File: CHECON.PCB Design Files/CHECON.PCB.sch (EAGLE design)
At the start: 24 parts, among them U2 MAX232SOIC16, U3 RS485SOIC

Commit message: CHECON.PCB.v1.0 pre-release
Pending checklist processing.
Added all part and manufacturer numbers, fiducials, silkscreen
labelling, BOM, ECO, FAB notes, Gerber files (+ drill and centroid)
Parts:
- added IC1: (no value), KW2:NCP1117ST33T3G_1
- added U$17, U$34: 1uF, GW-devices:RF-C0805
- added U$24, U$31, U$32, U$35: 10uF, GW-devices:RF-C0805
- added U$25, U$26, U$27, U$28, U$29, U$6: 10k, GW-devices:RF-R0805
- added U$30: RA_BUTTON, KW2:RA_BUTTON
- added U$33, U$7: 0.1uF, GW-devices:RF-C0805
- added U$36: 0, GW-devices:RF-R0805
- added U$37: DIODE-ZENER-BZT52, SparkFun:DIODE-ZENER-BZT52
- added U$38, U$39, U$40, U$41, U$42, U$43: FIDUCIAL, adafruit:FIDUCIAL
- POSCON: MFGN (none) -> Molex; MFGP (none) -> 0955016889
- SCANNER: MFGP (none) -> 0955016889
- U$1: MFGP (none) -> CLV1A-FKB-CK1N1G1BB7R4S3
- U$10: MFGP (none) -> DF12(3.0)-40DP-0.5V(86)
- U$11, U$12, U$21, U$22, U$23: value (none) -> 1uF; MFGN (none) -> TDK; MFGP (none) -> C2012X5R1E105K125AA
- U$13, U$14, U$15, U$16: MFGN (none) -> E-Switch; MFGP (none) -> TL3301DF160QG
- U$18, U$19, U$20: value (none) -> 24; MFGN (none) -> Vishay Dale; MFGP (none) -> CRCW080524R0FKEA
- U$2: value 52745-1097 -> (none); MFGP (none) -> 52745-1097
- U$3: MFGP (none) -> 3220-20-0100-00
- U$8: MFGP (none) -> WS2801
- U$9: MFGP (none) -> PJ-002A
- U2, U3: MFGN TI -> (none)
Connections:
- new net N$32: U$2.EXTMODE, U$6.1
- new net N$33: U$2.EXCOMIN, U$25.1
- new net N$34: U$10.PTE2/LLWU_P1/MADC0_DP1/SPI1_SCK/!UART1_CTS!/MTRACE_D2, U$16.4, U$26.1
- new net N$35: U$10.PTE17/ADC0_SE5A/SPI0_SCK/UART2_RX/FTM_CLKIN1/LPTMR0_ALT3, U$15.4, U$27.1
- new net N$36: U$10.PTE4/LLWU_P2/SPI1_PCS0/MTRACE_D0, U$14.4, U$28.1
- new net N$37: U$10.PTE16/ADC0_SE4A/SPI0_PCS0/UART2_TX/FTM_CLKIN0/FTM0_FLT3, U$13.4, U$29.1
- new net N$39: U$10.PTD4/LLWU_P14/MADC0_SE21/SPI0_PCS1/!UART0_RTS!/FTM0_CH4/EWM_IN/GPIO_BSM_FRAME, U$5.EN
- new net N$40: U$10.PTD3/SPI0_SIN/UART2_TX/I2C0_SCL/GPIO5_BSM_CLK, U$4.EN
- new net N$41: U$10.PTE3/MADC0_DM1/SPI1_SIN/!UART1_RTS!/MTRACE_D1/SPI1_SOUT, U2.T2IN
- new net OUT1: IC1.OUT, IC1.OUT1, U$32.2, U$36.1
- net +3V3: now also U$21.1, U$26.2, U$27.2, U$28.2, U$29.2, U$36.2, U$37.C, U2.VCC; no longer U$1.ANODE, U$8.VCC
- net GND: now also IC1.GND, U$13.1, U$13.2, U$14.1, U$14.2, U$15.1, U$15.2, U$16.1, U$16.2, U$17.2, U$2.VSS, U$2.VSSA, U$24.2, U$25.2, U$3.P$15, U$3.P$17, U$3.P$19, U$3.P$3, U$3.P$5, U$3.P$9, U$30.1, U$31.1, U$32.1, U$33.1, U$34.1, U$35.1, U$37.A, U$6.2, U$7.2
- net N$24: no longer U3.VCC
- net N$29: now also U$2.SI; no longer U$2.P$2
- net N$30: now also U$2.SCLK; no longer U$2.P$1
- net N$31: now also U$2.SCS; no longer U$2.P$3
- net N$6: now also U$30.2
- net N$7: now also SCANNER.6, U2.T2OUT; no longer U$3.P$15, U$3.P$17, U$3.P$19, U$3.P$3, U$3.P$5, U$3.P$9
- net V+: now also IC1.IN, U$1.ANODE, U$17.1, U$2.DISP, U$2.VDD, U$2.VDDA, U$24.1, U$31.2, U$33.2, U$34.2, U$35.2, U$7.1, U$8.VCC, U3.VCC; no longer U$10.VIN@1, U$10.VIN@2, U$21.1, U2.VCC
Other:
- moved on the sheet: SCANNER, U$11, U$12, U$13, U$14, U$15, U$16, U$21, U$22, U$23, U2

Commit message: CHECON.PCB.V1.0
Fixed some pin 1 markers, grounded unused input on 232, package names,
flipped FPC pins to correct pin 1 location
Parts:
- U$25, U$6: MFGP CRCW080568K0FKEA -> CRCW080510K0FKEA
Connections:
- net GND: now also U2.R2IN
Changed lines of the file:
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@@
 <part name="U$6" library="GW-devices" deviceset="RF-R" device="0805" value="10k">
 <attribute name="MFGN" value="Vishay Dale"/>
-<attribute name="MFGP" value="CRCW080568K0FKEA"/>
+<attribute name="MFGP" value="CRCW080510K0FKEA"/>
 </part>
 <part name="GND13" library="supply1" deviceset="GND" device=""/>
@@
 <part name="U$25" library="GW-devices" deviceset="RF-R" device="0805" value="10k">
 <attribute name="MFGN" value="Vishay Dale"/>
-<attribute name="MFGP" value="CRCW080568K0FKEA"/>
+<attribute name="MFGP" value="CRCW080510K0FKEA"/>
 </part>
 <part name="U$26" library="GW-devices" deviceset="RF-R" device="0805" value="10k">
@@
 <pinref part="U2" gate="G$1" pin="GND"/>
 <wire x1="-406.4" y1="134.62" x2="-406.4" y2="132.08" width="0.1524" layer="91"/>
-<wire x1="-406.4" y1="132.08" x2="-368.3" y2="132.08" width="0.1524" layer="91"/>
+<wire x1="-406.4" y1="132.08" x2="-386.08" y2="132.08" width="0.1524" layer="91"/>
+<wire x1="-386.08" y1="132.08" x2="-368.3" y2="132.08" width="0.1524" layer="91"/>
 <wire x1="-368.3" y1="132.08" x2="-368.3" y2="162.56" width="0.1524" layer="91"/>
 <junction x="-368.3" y="162.56"/>
@@
 <pinref part="U$22" gate="G$1" pin="2"/>
 <pinref part="U$23" gate="G$1" pin="2"/>
+<pinref part="U2" gate="G$1" pin="R2IN"/>
+<wire x1="-388.62" y1="142.24" x2="-386.08" y2="142.24" width="0.1524" layer="91"/>
+<wire x1="-386.08" y1="142.24" x2="-386.08" y2="132.08" width="0.1524" layer="91"/>
+<junction x="-386.08" y="132.08"/>
 </segment>
 <segment>
@@
 </sheet>
 </sheets>
+<errors>
+</errors>
 </schematic>
 </drawing>

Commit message: Backlight Routing
Added backlight drivers and power monitoring. Mid-routing.
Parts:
- added C11, C14: 0.1uF, GW-devices:RF-C0805
- added LQH3NPN100NM0L, U$47, U$49: 1212_IND, KW2:1212_IND
- added R10: (no value), GW-devices:RF-R2512
- added R12, R13: 10, GW-devices:RF-R0805
- added U$44: SC4541, KW2:SC4541
- added U$45: PCA9632DP1, KW2:PCA9632DP1
- added U$46: 10k, GW-devices:RF-R0805
- added U$50, U$51, U$52, U$53, U$54, U$55: 1uF, GW-devices:RF-C0805
- added U$56: 6.6, GW-devices:RF-R0805
- added U$57, U$58: 3.3, GW-devices:RF-R0805
- added U$59: BL_CON, KW2:BL_CON
- added U$60, U$61: 4.7k, GW-devices:RF-R0805
- added U$62: INA219B, texas:INA219B
- U$1: MFGP CLV1A-FKB-CK1N1G1BB7R4S3 -> (none)
- U$10: value DF12_F -> KW2_CPU_COMBO; device KW2:DF12_F -> KW2:KW2_CPU_COMBO; MFGP DF12(3.0)-40DP-0.5V(86) -> (none)
- U$2: value (none) -> 52745-1097; MFGP 52745-1097 -> (none)
- U$3: MFGP 3220-20-0100-00 -> (none)
- U$36: value 0 -> SC4541; device GW-devices:RF-R0805 -> KW2:SC4541; MFGN Vishay Dale -> (none); MFGP CRCW08050000Z0EAHP -> (none)
- U$37: value DIODE-ZENER-BZT52 -> SC4541; device SparkFun:DIODE-ZENER-BZT52 -> KW2:SC4541; NOTES DNP -> (none)
- U$9: MFGP PJ-002A -> (none)
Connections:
- removed net OUT1: IC1.OUT, IC1.OUT1, U$32.2, U$36.1
- new net N$38: U$10.PTE2/LLWU_P1/MADC0_DP1/SPI1_SCK/!UART1_CTS!/MTRACE_D2, U2.R2OUT
- new net N$42: U$10.PTA18/EXTAL0/FTM0_FTL2_FTM_CLKIN0, U$16.4, U$26.1
- new net N$43: U$36.EN, U$37.EN, U$44.EN, U$45.LED0, U$46.2
- new net N$44: U$37.SW, U$47.2, U$50.2
- new net N$45: U$10.PTD2/LLWU_P13/SPI0_SOUT/UART2_RX/I2C0_SDA/GPIO4_BSM_DATA, U$45.SDA, U$61.2, U$62.SDA
- new net N$46: LQH3NPN100NM0L.2, U$36.SW, U$52.2
- new net N$47: U$10.PTD3/SPI0_SIN/UART2_TX/I2C0_SCL/GPIO5_BSM_CLK, U$45.SCL, U$60.2, U$62.SCL
- new net N$48: U$44.SW, U$49.2, U$51.2
- new net N$50: U$44.FB, U$58.2
- new net N$51: U$44.OUT, U$55.1, U$58.1, U$59.A1
- new net N$52: U$37.FB, U$57.2
- new net N$53: U$37.OUT, U$54.1, U$57.1, U$59.A2
- new net N$54: U$36.OUT, U$53.1, U$56.1, U$59.A3
- new net N$55: U$36.FB, U$56.2
- new net N$56: C11.1, R12.1, U$62.VIN+
- new net N$57: C11.2, R13.1, U$62.VIN-
- new net N$58: IC1.IN, R10.2, R13.2, U$31.2
- net +3V3: now also C14.1, IC1.OUT, IC1.OUT1, LQH3NPN100NM0L.1, U$32.2, U$36.IN, U$37.IN, U$44.IN, U$45.VDD, U$47.1, U$49.1, U$60.1, U$61.1, U$62.VS; no longer U$36.2, U$37.C
- net GND: now also C14.2, U$36.GND, U$37.GND, U$44.GND, U$45.GND, U$46.1, U$50.1, U$51.1, U$52.1, U$53.2, U$54.2, U$55.2, U$59.GND, U$62.A0, U$62.A1, U$62.GND; no longer U$37.A, U2.R2IN
- net N$34: now also SCANNER.5, U2.R2IN; no longer U$10.PTE2/LLWU_P1/MADC0_DP1/SPI1_SCK/!UART1_CTS!/MTRACE_D2, U$16.4, U$26.1
- net N$40: now also U$10.PTA4/LLWU_P3/!NMI!/!EZP_CS!/FTM0_CH1; no longer U$10.PTD3/SPI0_SIN/UART2_TX/I2C0_SCL/GPIO5_BSM_CLK
- net V+: now also R10.1, R12.2; no longer IC1.IN, U$31.2
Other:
- moved on the sheet: IC1, U$17, U$24, U$31, U$32, U$33, U$34, U$35, U$7, U$9

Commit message: Finished layout pending spring connector
Waiting for physical location of BL connector
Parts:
- LQH3NPN100NM0L, U$47, U$49: MFGN (none) -> Murata; MFGP (none) -> LQH3NPN100NM0L
- U$56: value 6.6 -> 6.8; MFGN Vishay Dale -> Yageo; MFGP CRCW080510K0FKEA -> RC0805FR-076R8L
- U$57, U$58: MFGN Vishay Dale -> Samsung; MFGP CRCW080510K0FKEA -> RC2012F3R3CS
- U$60, U$61: MFGN Vishay Dale -> Panasonic; MFGP CRCW080510K0FKEA -> ERJ-6ENF4701V
- U$62: device texas:INA219B -> KW2:INA219B
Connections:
- removed net N$58: IC1.IN, R10.2, R13.2, U$31.2
- new net N$49: R10.1, R12.2, U$33.2, U$34.2, U$35.2, U$9.PWR
- net V+: now also IC1.IN, R10.2, R13.2, U$31.2; no longer R10.1, R12.2, U$33.2, U$34.2, U$35.2, U$9.PWR
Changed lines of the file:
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@@
 <part name="GND19" library="supply1" deviceset="GND" device=""/>
 <part name="GND20" library="supply1" deviceset="GND" device=""/>
-<part name="U$47" library="KW2" deviceset="1212_IND" device=""/>
-<part name="LQH3NPN100NM0L" library="KW2" deviceset="1212_IND" device=""/>
-<part name="U$49" library="KW2" deviceset="1212_IND" device=""/>
+<part name="U$47" library="KW2" deviceset="1212_IND" device="">
+<attribute name="MFGN" value="Murata"/>
+<attribute name="MFGP" value="LQH3NPN100NM0L"/>
+</part>
+<part name="LQH3NPN100NM0L" library="KW2" deviceset="1212_IND" device="">
+<attribute name="MFGN" value="Murata"/>
+<attribute name="MFGP" value="LQH3NPN100NM0L"/>
+</part>
+<part name="U$49" library="KW2" deviceset="1212_IND" device="">
+<attribute name="MFGN" value="Murata"/>
+<attribute name="MFGP" value="LQH3NPN100NM0L"/>
+</part>
 <part name="U$50" library="GW-devices" deviceset="RF-C" device="0805" value="1uF">
 <attribute name="MFGN" value="TDK"/>
@@
 <attribute name="MFGP" value="C2012X5R1E105K125AA"/>
 </part>
-<part name="U$56" library="GW-devices" deviceset="RF-R" device="0805" value="6.6">
-<attribute name="MFGN" value="Vishay Dale"/>
-<attribute name="MFGP" value="CRCW080510K0FKEA"/>
+<part name="U$56" library="GW-devices" deviceset="RF-R" device="0805" value="6.8">
+<attribute name="MFGN" value="Yageo"/>
+<attribute name="MFGP" value="RC0805FR-076R8L"/>
 </part>
 <part name="U$57" library="GW-devices" deviceset="RF-R" device="0805" value="3.3">
-<attribute name="MFGN" value="Vishay Dale"/>
-<attribute name="MFGP" value="CRCW080510K0FKEA"/>
+<attribute name="MFGN" value="Samsung"/>
+<attribute name="MFGP" value="RC2012F3R3CS"/>
 </part>
 <part name="U$58" library="GW-devices" deviceset="RF-R" device="0805" value="3.3">
-<attribute name="MFGN" value="Vishay Dale"/>
-<attribute name="MFGP" value="CRCW080510K0FKEA"/>
+<attribute name="MFGN" value="Samsung"/>
+<attribute name="MFGP" value="RC2012F3R3CS"/>
 </part>
 <part name="GND21" library="supply1" deviceset="GND" device=""/>
@@
 <part name="+3V8" library="supply1" deviceset="+3V3" device=""/>
 <part name="U$60" library="GW-devices" deviceset="RF-R" device="0805" value="4.7k">
-<attribute name="MFGN" value="Vishay Dale"/>
-<attribute name="MFGP" value="CRCW080510K0FKEA"/>
+<attribute name="MFGN" value="Panasonic"/>
+<attribute name="MFGP" value="ERJ-6ENF4701V"/>
 </part>
 <part name="U$61" library="GW-devices" deviceset="RF-R" device="0805" value="4.7k">
-<attribute name="MFGN" value="Vishay Dale"/>
-<attribute name="MFGP" value="CRCW080510K0FKEA"/>
+<attribute name="MFGN" value="Panasonic"/>
+<attribute name="MFGP" value="ERJ-6ENF4701V"/>
 </part>
 <part name="+3V9" library="supply1" deviceset="+3V3" device=""/>
 <part name="R10" library="GW-devices" deviceset="RF-R" device="2512"/>
-<part name="U$62" library="texas" deviceset="INA219B" device=""/>
+<part name="U$62" library="KW2" deviceset="INA219B" device=""/>
 <part name="GND28" library="supply1" deviceset="GND" device=""/>
 <part name="+3V10" library="supply1" deviceset="+3V3" device=""/>
@@
 <instance part="+3V7" gate="G$1" x="-73.66" y="114.3"/>
 <instance part="GND3" gate="1" x="-50.8" y="231.14"/>
-<instance part="SUPPLY1" gate="1" x="-60.96" y="238.76"/>
+<instance part="SUPPLY1" gate="1" x="-101.6" y="246.38"/>
 <instance part="+3V1" gate="G$1" x="-195.58" y="149.86"/>
 <instance part="GND7" gate="1" x="-149.86" y="86.36"/>
@@
 <instance part="GND19" gate="1" x="-129.54" y="10.16"/>
 <instance part="GND20" gate="1" x="-91.44" y="-5.08"/>
-<instance part="U$47" gate="G$1" x="-198.12" y="0" rot="R180"/>
-<instance part="LQH3NPN100NM0L" gate="G$1" x="-198.12" y="38.1" rot="R180"/>
-<instance part="U$49" gate="G$1" x="-195.58" y="-38.1" rot="R180"/>
+<instance part="U$47" gate="G$1" x="-198.12" y="0" rot="R180">
+<attribute name="MFGN" x="-198.12" y="0" size="1.778" layer="96" rot="R180" display="off"/>
+<attribute name="MFGP" x="-198.12" y="0" size="1.778" layer="96" rot="R180" display="off"/>
+</instance>
+<instance part="LQH3NPN100NM0L" gate="G$1" x="-198.12" y="38.1" rot="R180">
+<attribute name="MFGN" x="-198.12" y="38.1" size="1.778" layer="96" rot="R180" display="off"/>
+<attribute name="MFGP" x="-198.12" y="38.1" size="1.778" layer="96" rot="R180" display="off"/>
+</instance>
+<instance part="U$49" gate="G$1" x="-195.58" y="-38.1" rot="R180">
+<attribute name="MFGN" x="-195.58" y="-38.1" size="1.778" layer="96" rot="R180" display="off"/>
+<attribute name="MFGP" x="-195.58" y="-38.1" size="1.778" layer="96" rot="R180" display="off"/>
+</instance>
 <instance part="U$50" gate="G$1" x="-187.96" y="2.54" rot="R180">
 <attribute name="MFGP" x="-187.96" y="2.54" size="1.778" layer="96" rot="R180" display="off"/>
@@
 <net name="V+" class="0">
 <segment>
-<pinref part="U$9" gate="G$1" pin="PWR"/>
-<wire x1="-45.72" y1="226.06" x2="-40.64" y2="226.06" width="0.1524" layer="91"/>
-<pinref part="U$35" gate="G$1" pin="2"/>
-<junction x="-45.72" y="226.06"/>
-<pinref part="SUPPLY1" gate="1" pin="V+"/>
-<wire x1="-60.96" y1="236.22" x2="-60.96" y2="233.68" width="0.1524" layer="91"/>
-<wire x1="-60.96" y1="233.68" x2="-60.96" y2="226.06" width="0.1524" layer="91"/>
-<wire x1="-60.96" y1="226.06" x2="-55.88" y2="226.06" width="0.1524" layer="91"/>
-<pinref part="U$33" gate="G$1" pin="2"/>
-<junction x="-55.88" y="226.06"/>
-<wire x1="-55.88" y1="226.06" x2="-50.8" y2="226.06" width="0.1524" layer="91"/>
-<wire x1="-50.8" y1="226.06" x2="-45.72" y2="226.06" width="0.1524" layer="91"/>
-<pinref part="U$34" gate="G$1" pin="2"/>
-<junction x="-50.8" y="226.06"/>
-<wire x1="-60.96" y1="233.68" x2="-68.58" y2="233.68" width="0.1524" layer="91"/>
-<junction x="-60.96" y="233.68"/>
-<wire x1="-68.58" y1="233.68" x2="-71.12" y2="233.68" width="0.1524" layer="91"/>
-<wire x1="-71.12" y1="233.68" x2="-71.12" y2="241.3" width="0.1524" layer="91"/>
-<pinref part="R10" gate="&gt;NAME" pin="1"/>
-<wire x1="-81.28" y1="241.3" x2="-76.2" y2="241.3" width="0.1524" layer="91"/>
-<pinref part="R12" gate="&gt;NAME" pin="2"/>
-<wire x1="-76.2" y1="241.3" x2="-76.2" y2="236.22" width="0.1524" layer="91"/>
-<wire x1="-71.12" y1="241.3" x2="-76.2" y2="241.3" width="0.1524" layer="91"/>
-<junction x="-76.2" y="241.3"/>
-</segment>
-<segment>
 <pinref part="SUPPLY4" gate="1" pin="V+"/>
 <wire x1="-335.28" y1="91.44" x2="-335.28" y2="86.36" width="0.1524" layer="91"/>
@@
 <pinref part="SUPPLY8" gate="1" pin="V+"/>
 </segment>
+<segment>
+<pinref part="U$31" gate="G$1" pin="2"/>
+<pinref part="IC1" gate="G$1" pin="IN"/>
+<wire x1="-116.84" y1="238.76" x2="-111.76" y2="238.76" width="0.1524" layer="91"/>
+<pinref part="R10" gate="&gt;NAME" pin="2"/>
+<pinref part="R13" gate="&gt;NAME" pin="2"/>
+<wire x1="-93.98" y1="241.3" x2="-91.44" y2="241.3" width="0.1524" layer="91"/>
+<wire x1="-93.98" y1="241.3" x2="-93.98" y2="238.76" width="0.1524" layer="91"/>
+<wire x1="-93.98" y1="238.76" x2="-93.98" y2="236.22" width="0.1524" layer="91"/>
+<wire x1="-111.76" y1="238.76" x2="-101.6" y2="238.76" width="0.1524" layer="91"/>
+<junction x="-111.76" y="238.76"/>
+<junction x="-93.98" y="238.76"/>
+<pinref part="SUPPLY1" gate="1" pin="V+"/>
+<wire x1="-101.6" y1="238.76" x2="-93.98" y2="238.76" width="0.1524" layer="91"/>
+<wire x1="-101.6" y1="243.84" x2="-101.6" y2="238.76" width="0.1524" layer="91"/>
+<junction x="-101.6" y="238.76"/>
+</segment>
 </net>
 <net name="N$13" class="0">
@@
 </segment>
 </net>
-<net name="N$58" class="0">
-<segment>
-<pinref part="U$31" gate="G$1" pin="2"/>
-<pinref part="IC1" gate="G$1" pin="IN"/>
-<wire x1="-116.84" y1="238.76" x2="-111.76" y2="238.76" width="0.1524" layer="91"/>
-<pinref part="R10" gate="&gt;NAME" pin="2"/>
-<pinref part="R13" gate="&gt;NAME" pin="2"/>
-<wire x1="-93.98" y1="241.3" x2="-91.44" y2="241.3" width="0.1524" layer="91"/>
-<wire x1="-93.98" y1="241.3" x2="-93.98" y2="238.76" width="0.1524" layer="91"/>
-<wire x1="-93.98" y1="238.76" x2="-93.98" y2="236.22" width="0.1524" layer="91"/>
-<wire x1="-111.76" y1="238.76" x2="-93.98" y2="238.76" width="0.1524" layer="91"/>
-<junction x="-111.76" y="238.76"/>
-<junction x="-93.98" y="238.76"/>
-</segment>
-</net>
+<net name="N$49" class="0">
+<segment>
+<pinref part="U$9" gate="G$1" pin="PWR"/>
+<wire x1="-45.72" y1="226.06" x2="-40.64" y2="226.06" width="0.1524" layer="91"/>
+<pinref part="U$35" gate="G$1" pin="2"/>
+<junction x="-45.72" y="226.06"/>
+<wire x1="-60.96" y1="233.68" x2="-60.96" y2="226.06" width="0.1524" layer="91"/>
+<wire x1="-60.96" y1="226.06" x2="-55.88" y2="226.06" width="0.1524" layer="91"/>
+<pinref part="U$33" gate="G$1" pin="2"/>
+<junction x="-55.88" y="226.06"/>
+<wire x1="-55.88" y1="226.06" x2="-50.8" y2="226.06" width="0.1524" layer="91"/>
+<wire x1="-50.8" y1="226.06" x2="-45.72" y2="226.06" width="0.1524" layer="91"/>
+<pinref part="U$34" gate="G$1" pin="2"/>
+<junction x="-50.8" y="226.06"/>
+<wire x1="-60.96" y1="233.68" x2="-68.58" y2="233.68" width="0.1524" layer="91"/>
+<wire x1="-68.58" y1="233.68" x2="-71.12" y2="233.68" width="0.1524" layer="91"/>
+<wire x1="-71.12" y1="233.68" x2="-71.12" y2="241.3" width="0.1524" layer="91"/>
+<pinref part="R10" gate="&gt;NAME" pin="1"/>
+<wire x1="-81.28" y1="241.3" x2="-76.2" y2="241.3" width="0.1524" layer="91"/>
+<pinref part="R12" gate="&gt;NAME" pin="2"/>
+<wire x1="-76.2" y1="241.3" x2="-76.2" y2="236.22" width="0.1524" layer="91"/>
+<wire x1="-71.12" y1="241.3" x2="-76.2" y2="241.3" width="0.1524" layer="91"/>
+<junction x="-76.2" y="241.3"/>
+</segment>
+</net>

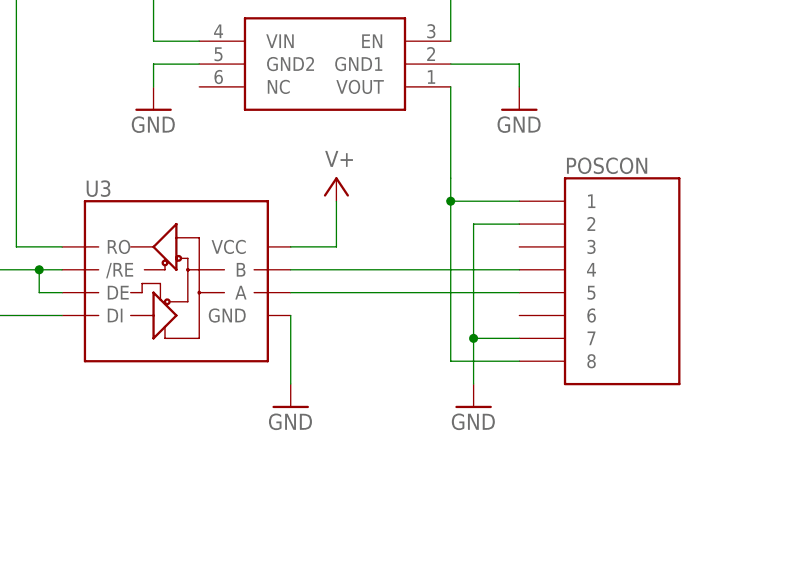
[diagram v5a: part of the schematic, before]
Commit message: Added bus terminator to schematic
Still need to add to layout
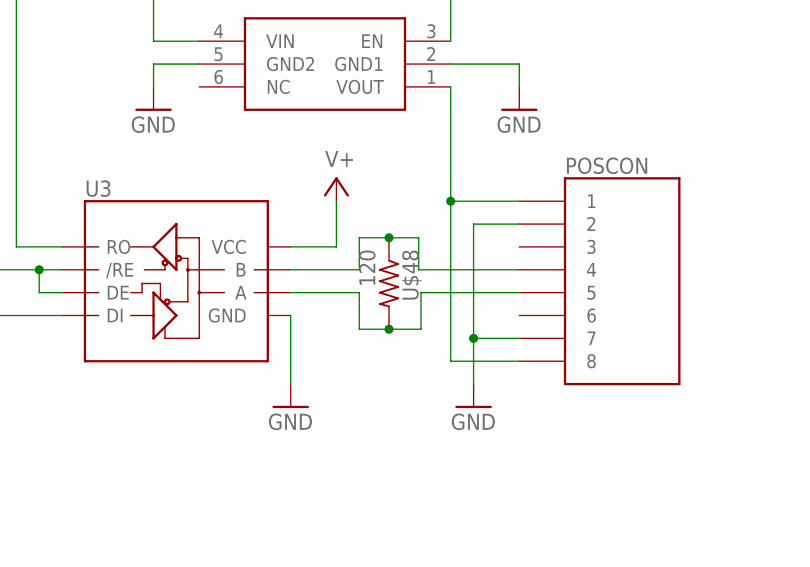
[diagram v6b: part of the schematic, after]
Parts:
- added U$48: 120, GW-devices:RF-R0805
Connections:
- net N$19: now also U$48.1
- net N$20: now also U$48.2
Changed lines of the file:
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@@
 <part name="C14" library="GW-devices" deviceset="RF-C" device="0805" value="0.1uF"/>
 <part name="GND29" library="supply1" deviceset="GND" device=""/>
+<part name="U$48" library="GW-devices" deviceset="RF-R" device="0805" value="120">
+<attribute name="MFGN" value="Panasonic"/>
+<attribute name="MFGP" value="ERJ-6ENF4701V"/>
+</part>
 </parts>
 <sheets>
@@
 <instance part="C14" gate="G$1" x="-71.12" y="180.34" rot="MR270"/>
 <instance part="GND29" gate="1" x="-114.3" y="195.58" rot="MR0"/>
+<instance part="U$48" gate="&gt;NAME" x="-309.118" y="59.436" rot="R270">
+<attribute name="MFGP" x="-309.118" y="59.436" size="1.778" layer="96" rot="R270" display="off"/>
+<attribute name="MFGN" x="-309.118" y="59.436" size="1.778" layer="96" rot="R270" display="off"/>
+</instance>
 </instances>
 <busses>
@@
 </segment>
 </net>
-<net name="N$19" class="0">
-<segment>
-<pinref part="U3" gate="G$1" pin="B"/>
-<pinref part="POSCON" gate="G$1" pin="4"/>
-<wire x1="-320.04" y1="60.96" x2="-294.64" y2="60.96" width="0.1524" layer="91"/>
-</segment>
-</net>
-<net name="N$20" class="0">
-<segment>
-<pinref part="U3" gate="G$1" pin="A"/>
-<pinref part="POSCON" gate="G$1" pin="5"/>
-<wire x1="-320.04" y1="58.42" x2="-294.64" y2="58.42" width="0.1524" layer="91"/>
-</segment>
-</net>
 <net name="N$18" class="0">
 <segment>
@@
 </segment>
 </net>
+<net name="N$19" class="0">
+<segment>
+<pinref part="U3" gate="G$1" pin="B"/>
+<wire x1="-320.04" y1="60.96" x2="-312.42" y2="60.96" width="0.1524" layer="91"/>
+<wire x1="-312.42" y1="60.96" x2="-312.42" y2="64.516" width="0.1524" layer="91"/>
+<pinref part="U$48" gate="&gt;NAME" pin="1"/>
+<wire x1="-312.42" y1="64.516" x2="-309.118" y2="64.516" width="0.1524" layer="91"/>
+<wire x1="-309.118" y1="64.516" x2="-305.816" y2="64.516" width="0.1524" layer="91"/>
+<junction x="-309.118" y="64.516"/>
+<wire x1="-305.816" y1="64.516" x2="-305.816" y2="60.96" width="0.1524" layer="91"/>
+<pinref part="POSCON" gate="G$1" pin="4"/>
+<wire x1="-305.816" y1="60.96" x2="-294.64" y2="60.96" width="0.1524" layer="91"/>
+</segment>
+</net>
+<net name="N$20" class="0">
+<segment>
+<pinref part="U3" gate="G$1" pin="A"/>
+<wire x1="-320.04" y1="58.42" x2="-312.42" y2="58.42" width="0.1524" layer="91"/>
+<wire x1="-312.42" y1="58.42" x2="-312.42" y2="54.356" width="0.1524" layer="91"/>
+<pinref part="U$48" gate="&gt;NAME" pin="2"/>
+<wire x1="-312.42" y1="54.356" x2="-309.118" y2="54.356" width="0.1524" layer="91"/>
+<pinref part="POSCON" gate="G$1" pin="5"/>
+<wire x1="-294.64" y1="58.42" x2="-305.562" y2="58.42" width="0.1524" layer="91"/>
+<wire x1="-305.562" y1="58.42" x2="-305.562" y2="54.356" width="0.1524" layer="91"/>
+<wire x1="-305.562" y1="54.356" x2="-309.118" y2="54.356" width="0.1524" layer="91"/>
+<junction x="-309.118" y="54.356"/>
+</segment>
+</net>
